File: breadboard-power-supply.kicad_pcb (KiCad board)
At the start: 2 copper layers, 53 x 30 mm, 28 parts, among them J1 PJ-002A, J2 PJ-002A, J3 TSW-102-07-F-S, J4 TSW-102-07-F-S, J5 TSW-102-07-F-S, J6 TSW-102-07-F-S, SW1 EG1271, SW2 EG2315, SW3 EG2315, U1 LM317M

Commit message: fixed date on board
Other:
- board text added: "2024-10-14"
- board text removed: "2024-10-02"
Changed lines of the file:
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@@
 			(drillshape 0)
 			(scaleselection 1)
-			(outputdirectory "exports/gerbers/")
+			(outputdirectory "manufacturing/fabrication/gerbers/")
 		)
 	)
@@
 		(layer "Edge.Cuts")
 	)
-	(gr_text "2024-10-02"
+	(gr_text "2024-10-14"
 		(at 126.5 91 0)
 		(layer "B.SilkS")

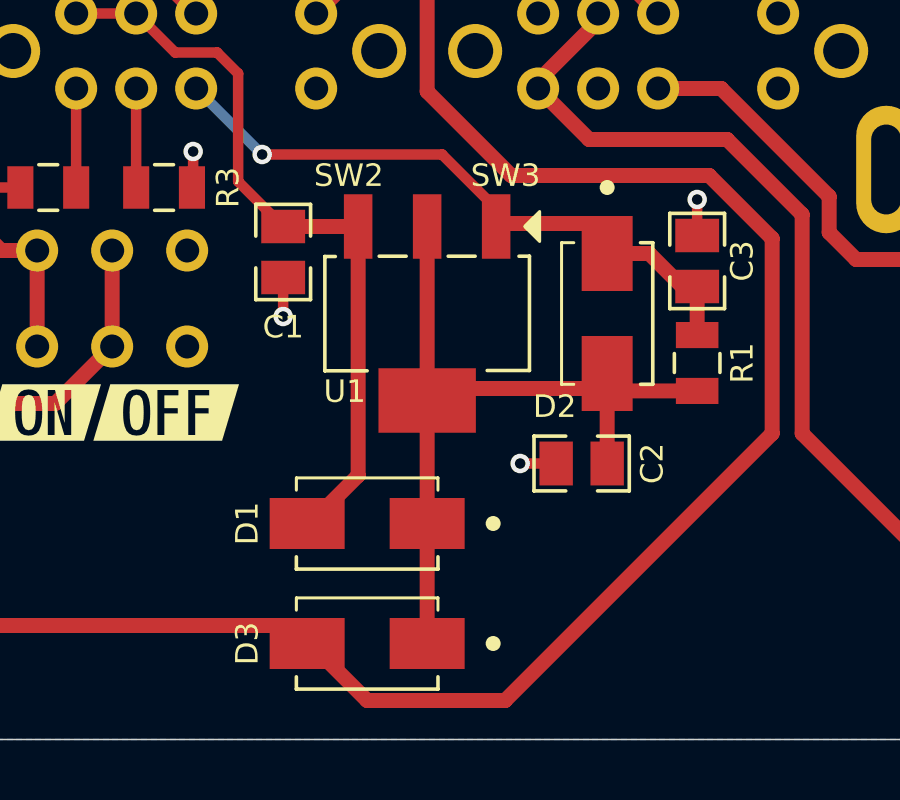
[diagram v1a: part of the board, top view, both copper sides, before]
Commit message: fixed diodes rotation and fixed voltage divider
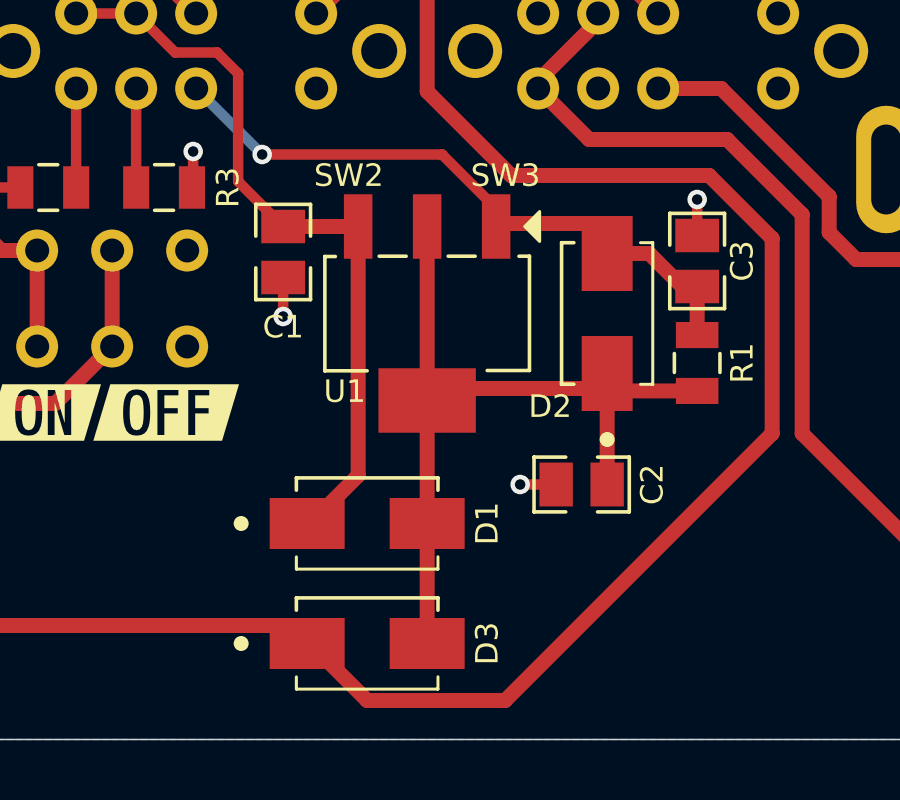
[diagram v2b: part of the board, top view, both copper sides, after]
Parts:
- R1: value 240R -> 280R
- R2: value 787R -> 510R
- R3: value 464R -> 887R
- moved C2 0.70 mm to (131.7, 111.5)
- turned D1 to 0 degrees
- turned D2 to 90 degrees
- turned D3 to 0 degrees
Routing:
- net Net-(C2-Pad1): track 26.5 -> 27.2 mm

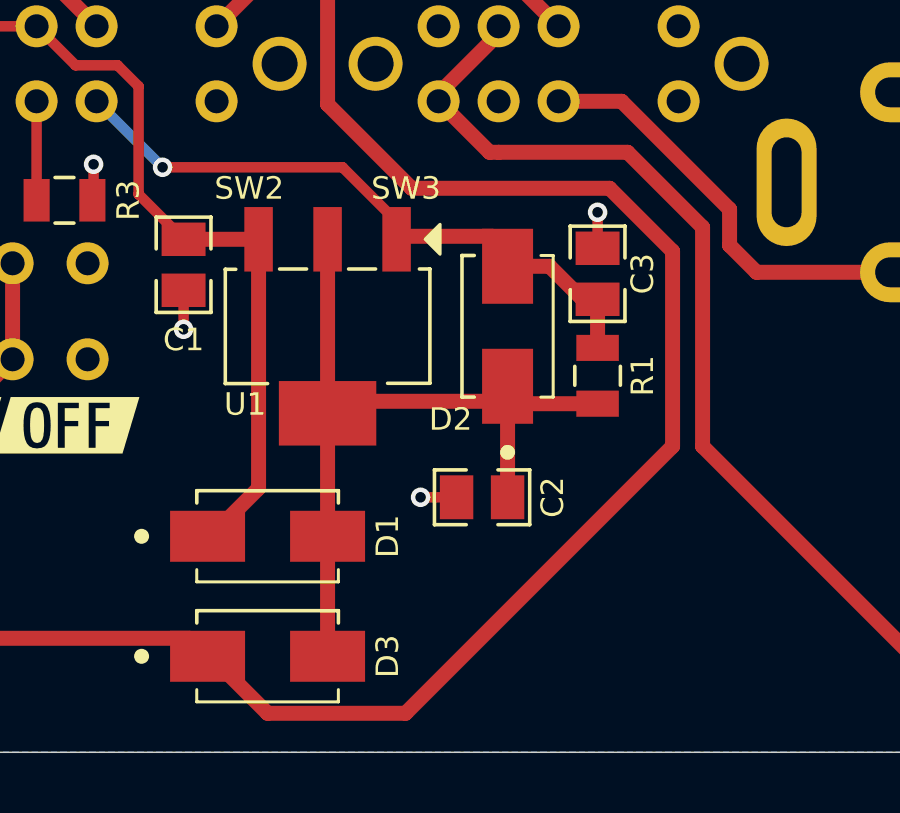
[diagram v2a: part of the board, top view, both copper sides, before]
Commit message: fixed sheet date and equation
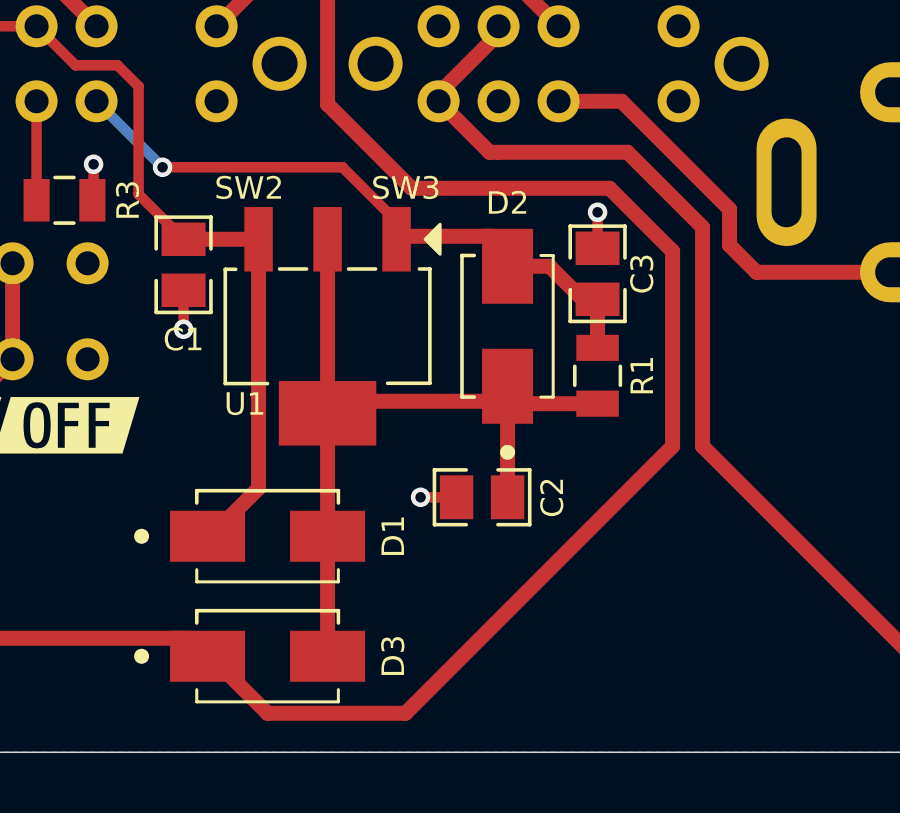
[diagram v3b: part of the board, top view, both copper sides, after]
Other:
- board text added: "2024-11-11"
- board text removed: "2024-10-14"
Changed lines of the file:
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@@
 	(title_block
 		(title "Breadboard Power Supply")
-		(date "2024-10-14")
+		(date "2024-11-11")
 		(comment 2 "PROTOTYPE")
 		(comment 3 "2024")
@@
 		(descr "Diode, Small Outline Diode (SOD); 2.50 mm L X 1.3 mm W X 1.05 mm H body")
 		(property "Reference" "D2"
-			(at -3.1 -1.9 360)
+			(at 4.1 0 0)
 			(layer "F.SilkS")
 			(effects
@@
 		(descr "Diode, Small Outline Diode (SOD); 2.50 mm L X 1.3 mm W X 1.05 mm H body")
 		(property "Reference" "D1"
-			(at 4 0 90)
+			(at 4.2 0 90)
 			(layer "F.SilkS")
 			(effects
@@
 		)
 		(property "Value" "ES1B-13-F"
-			(at 0 0 360)
+			(at 0 0 0)
 			(layer "F.Fab")
 			(hide yes)
@@
 		)
 		(property "Footprint" "lib_fp:SMA"
-			(at 0 -5.05 360)
+			(at 0 -5.05 0)
 			(layer "F.Fab")
 			(hide yes)
@@
 		)
 		(property "Datasheet" "datasheets/Diodes-Incorporated-ES1A--ES1G.pdf"
-			(at 0 -5.05 360)
+			(at 0 -5.05 0)
 			(layer "F.Fab")
 			(hide yes)
@@
 		)
 		(property "Description" "General diode"
-			(at 0 -5.05 360)
+			(at 0 -5.05 0)
 			(layer "F.Fab")
 			(hide yes)
@@
 		)
 		(fp_text user "${REFERENCE}"
-			(at 0 0 360)
+			(at 0 0 0)
 			(layer "F.Fab")
 			(hide yes)
@@
 		(descr "Diode, Small Outline Diode (SOD); 2.50 mm L X 1.3 mm W X 1.05 mm H body")
 		(property "Reference" "D3"
-			(at 4 0 90)
+			(at 4.2 0 90)
 			(layer "F.SilkS")
 			(effects
@@
 		)
 		(property "Value" "B140-13-F"
-			(at 0 0 360)
+			(at 0 0 0)
 			(layer "F.Fab")
 			(hide yes)
@@
 		)
 		(property "Footprint" "lib_fp:SMA"
-			(at 0 -5.05 360)
+			(at 0 -5.05 0)
 			(layer "F.Fab")
 			(hide yes)
@@
 		)
 		(property "Datasheet" "datasheets/Diodes-Incorporated-B120B-B160B.pdf"
-			(at 0 -5.05 360)
+			(at 0 -5.05 0)
 			(layer "F.Fab")
 			(hide yes)
@@
 		)
 		(property "Description" "DIODE SCHOTTKY 40V 1A SMA"
-			(at 0 -5.05 360)
+			(at 0 -5.05 0)
 			(layer "F.Fab")
 			(hide yes)
@@
 		)
 		(fp_text user "${REFERENCE}"
-			(at 0 0 360)
+			(at 0 0 0)
 			(layer "F.Fab")
 			(hide yes)
@@
 		(layer "Edge.Cuts")
 	)
-	(gr_text "2024-10-14"
+	(gr_text "2024-11-11"
 		(at 126.5 91 0)
 		(layer "B.SilkS")
